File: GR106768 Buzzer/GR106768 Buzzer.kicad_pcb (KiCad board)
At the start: 4 copper layers, 76 x 58 mm, 175 parts, among them IC1 L-BC-SOT23-5, IC2 L-BC-SO08, IC3 L-BC-SO08, IC4 L-BC-SOT23-5, IC5 L-BC-SO08, IC6 L-BC-SO08, IC7 L-BC-SOT23-6, IC8 L-BC-DFN10, IC9 L-BC-SOT23-6, J1 BAR-10-1007, J2 MIRECMS, J3 MIRECMS, SW1 SI-10-NK236, T1 Q-BC-SOT23-BEC, T10 Q-BC-SOT23-GSD, T11 Q-BC-SOT23-GSD, T12 Q-BC-SOT23-GSD, T13 Q-BC-SOT23-GSD, T2 Q-BC-SOT23-BEC, T3 Q-BC-SOT23-BEC, T4 Q-BC-SOT23-BEC, T5 Q-BC-SOT23-GSD, T6 Q-BC-SOT23-GSD, T7 Q-BC-SOT23-GSD, T8 Q-BC-SOT23-GSD, T9 Q-BC-SOT23-GSD

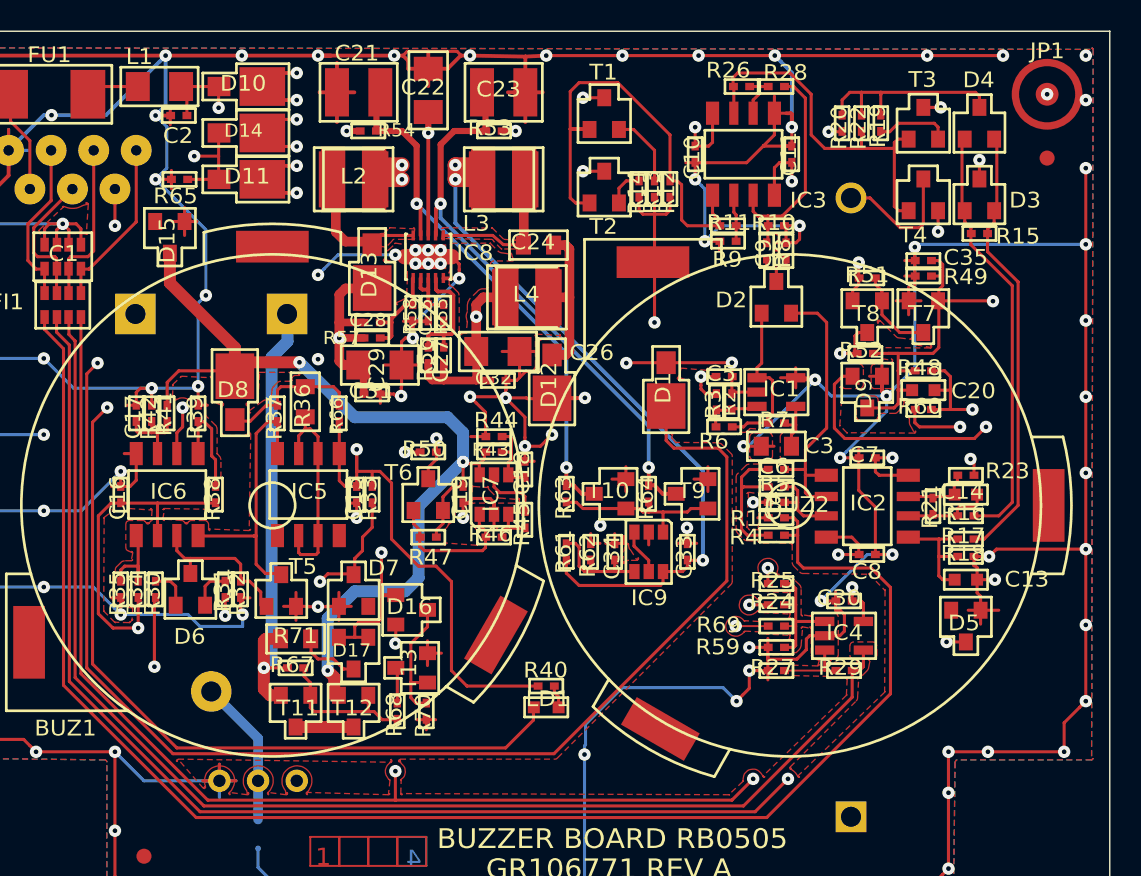
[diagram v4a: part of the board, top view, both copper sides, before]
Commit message: buzzer board custom via footprints
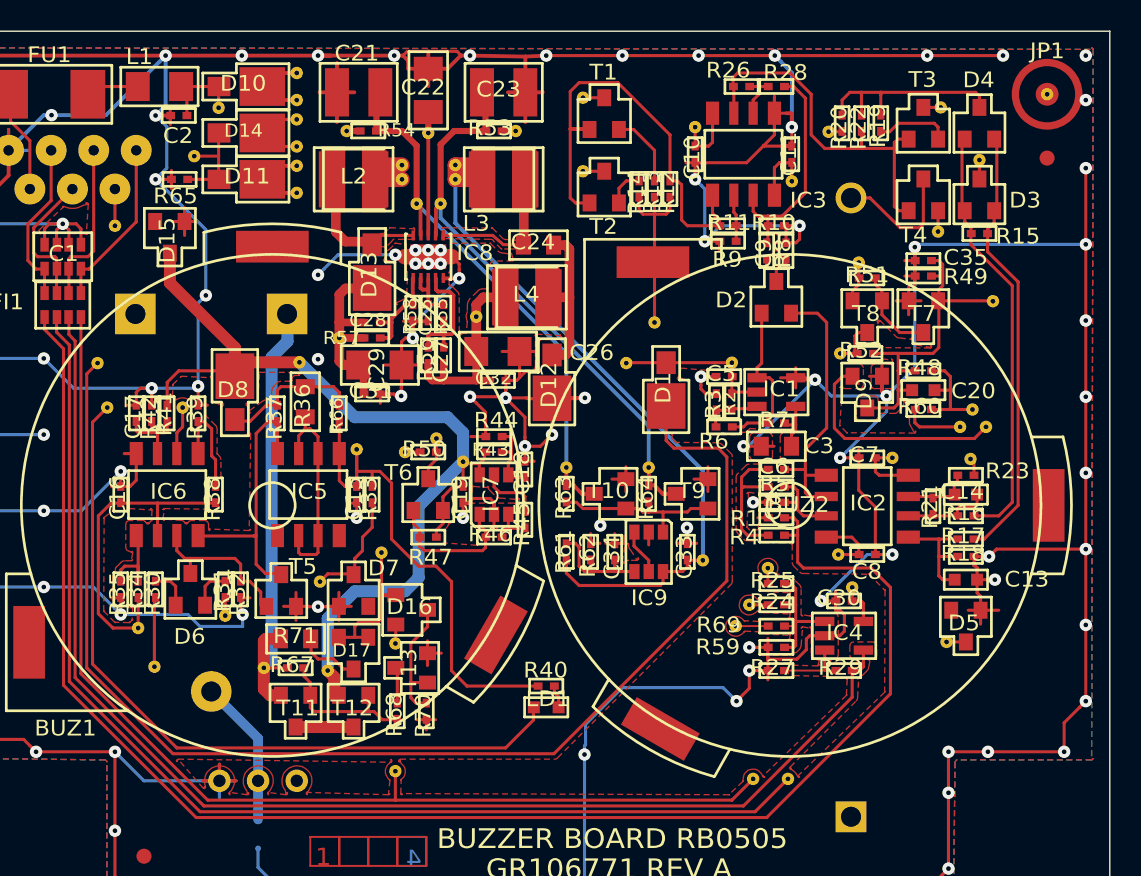
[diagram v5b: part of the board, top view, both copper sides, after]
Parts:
- added V1: +5V, AllModules:Via_12x32-1._.3.4, F.Cu at (143.2, 99.6)
- added V10: SUPPLY-BUZ-CPU, AllModules:Via_12x32-1._.3.4, F.Cu at (125.7, 78.2)
- added V11: SUPPLY-BUZ-CPU, AllModules:Via_12x32-1._.3.4, F.Cu at (124.6, 87.2)
- added V12: -12V, AllModules:Via_12x32-1._.3.4, F.Cu at (156.4, 74.6)
- added V13: -12V, AllModules:Via_12x32-1._.3.4, F.Cu at (170.1, 75.2)
- added V14: -12V, AllModules:Via_12x32-1._.3.4, F.Cu at (149.4, 84.1)
- added V15: -12V, AllModules:Via_12x32-1._.3.4, F.Cu at (173.2, 99.8)
- added V16: N$78, AllModules:Via_12x32-1._.3.4, F.Cu at (130.1, 90.1)
- added V17: N$78, AllModules:Via_12x32-1._.3.4, F.Cu at (125.2, 90.1)
- added V18: N$58, AllModules:Via_12x32-1._.3.4, F.Cu at (139.2, 101.5)
- added V19: N$58, AllModules:Via_12x32-1._.3.4, F.Cu at (127.2, 104.6)
- added V2: +5V, AllModules:Via_12x32-1._.3.4, F.Cu at (132.5, 70.4)
- added V20: N$31, AllModules:Via_12x32-1._.3.4, F.Cu at (182.5, 73.8)
- added V21: GT1, AllModules:Via_12x32-1._.3.4, F.Cu at (183.4, 83.1)
- added V22: GT1, AllModules:Via_12x32-1._.3.4, F.Cu at (186.9, 69.5)
- added V23: +12V, AllModules:Via_12x32-1._.3.4, F.Cu at (156.4, 69.8)
- added V24: +12V, AllModules:Via_12x32-1._.3.4, F.Cu at (179.9, 70.4)
- added V25: +12V, AllModules:Via_12x32-1._.3.4, F.Cu at (163.8, 71.7)
- added V26: +12V, AllModules:Via_12x32-1._.3.4, F.Cu at (140.4, 85.5)
- added V27: +12V, AllModules:Via_12x32-1._.3.4, F.Cu at (141.6, 92.8)
- added V28: +12V, AllModules:Via_12x32-1._.3.4, F.Cu at (176.8, 93.4)
- added V29: BATTV, AllModules:Via_12x32-1._._.4, F.Cu at (135.5, 107.2)
- added V3: +5V, AllModules:Via_12x32-1._.3.4, F.Cu at (181.2, 91.4)
- added V30: N$19, AllModules:Via_12x32-1._.3.4, F.Cu at (161.1, 84.5)
- added V31: N$18, AllModules:Via_12x32-1._.3.4, F.Cu at (172.6, 72.0)
- added V32: N$18, AllModules:Via_12x32-1._.3.4, F.Cu at (179.7, 78.5)
- added V33: N$10, AllModules:Via_12x32-1._._.4, F.Cu at (164.3, 100.1)
- added V34: N$10, AllModules:Via_12x32-1._.3.4, F.Cu at (148.0, 75.1)
- added V35: N$10, AllModules:Via_12x32-1._.3.4, F.Cu at (144.5, 75.1)
- added V36: N$10, AllModules:Via_12x32-1._.3.4, F.Cu at (144.5, 74.2)
- added V37: N$10, AllModules:Via_12x32-1._.3.4, F.Cu at (140.9, 71.9)
- added V38: N$10, AllModules:Via_12x32-1._.3.4, F.Cu at (146.3, 72.1)
- added V39: N$10, AllModules:Via_12x32-1._.3.4, F.Cu at (152.0, 71.9)
- added V4: +5V, AllModules:Via_12x32-1._.3.4, F.Cu at (144.7, 93.0)
- added V40: N$10, AllModules:Via_12x32-1._.3.4, F.Cu at (148.0, 74.2)
- added V41: N$10, AllModules:Via_12x32-1._.3.4, F.Cu at (137.6, 68.1)
- added V42: N$10, AllModules:Via_12x32-1._.3.4, F.Cu at (137.6, 69.9)
- added V43: N$10, AllModules:Via_12x32-1._.3.4, F.Cu at (137.6, 71.2)
- added V44: N$10, AllModules:Via_12x32-1._.3.4, F.Cu at (137.6, 73.0)
- added V45: N$10, AllModules:Via_12x32-1._.3.4, F.Cu at (137.6, 74.2)
- added V46: N$10, AllModules:Via_12x32-1._.3.4, F.Cu at (137.6, 76.0)
- added V47: STOP-INV, AllModules:Via_12x32-1._.3.4, F.Cu at (182.0, 90.2)
- added V48: STOP-INV, AllModules:Via_12x32-1._.3.4, F.Cu at (169.9, 114.5)
- added V49: VCHARG, AllModules:Via_12x32-1._._.4, F.Cu at (137.8, 87.1)
- added V5: +5V, AllModules:Via_12x32-1._.3.4, F.Cu at (174.1, 101.9)
- added V50: VCHARG, AllModules:Via_12x32-1._.3.4, F.Cu at (166.5, 104.5)
- added V51: VCHARG, AllModules:Via_12x32-1._.3.4, F.Cu at (139.7, 107.4)
- added V52: VCHARG, AllModules:Via_12x32-1._._.4, F.Cu at (148.6, 93.7)
- added V53: VBAT, AllModules:Via_12x32-1._.3.4, F.Cu at (174.5, 80.6)
- added V54: VBAT, AllModules:Via_12x32-1._.3.4, F.Cu at (146.8, 92.1)
- added V55: VBAT, AllModules:Via_12x32-1._.3.4, F.Cu at (168.6, 100.6)
- added V56: SUPPLY-BUZ, AllModules:Via_12x32-1._.3.4, F.Cu at (130.9, 73.6)
- added V57: SUPPLY-BUZ, AllModules:Via_12x32-1._.3.4, F.Cu at (173.3, 86.5)
- added V58: SUPPLY-BUZ, AllModules:Via_12x32-1._.3.4, F.Cu at (166.2, 87.2)
- added V59: SUPPLY-BUZ, AllModules:Via_12x32-1._.3.4, F.Cu at (159.3, 87.2)
- added V6: BUZ-ACT, AllModules:Via_12x32-1._.3.4, F.Cu at (128.3, 107.1)
- added V60: SUPPLY-BUZ, AllModules:Via_12x32-1._.3.4, F.Cu at (132.9, 103.8)
- added V61: SHDN2, AllModules:Via_12x32-1._._.4, F.Cu at (160.7, 94.0)
- added V62: SHDN2, AllModules:Via_12x32-1._._.4, F.Cu at (147.1, 76.7)
- added V63: SHDN1, AllModules:Via_12x32-1._._.4, F.Cu at (155.3, 94.0)
- added V64: SHDN1, AllModules:Via_12x32-1._._.4, F.Cu at (145.5, 76.7)
- added V65: INHIB-STOP-INV, AllModules:Via_12x32-1._.3.4, F.Cu at (144.1, 114.0)
- added V66: INHIB-STOP-INV, AllModules:Via_12x32-1._.3.4, F.Cu at (144.1, 105.6)
- added V67: INHIB-STOP-INV, AllModules:Via_12x32-1._.3.4, F.Cu at (182.9, 91.4)
- added V68: INHIB-STOP-INV, AllModules:Via_12x32-1._.3.4, F.Cu at (167.6, 114.5)
- added V7: BUZ-ACT, AllModules:Via_12x32-1._.3.4, F.Cu at (181.9, 93.5)
- added V8: BUZ-ACT, AllModules:Via_12x32-1._.3.4, F.Cu at (167.4, 103.1)
- added V9: BUZ-ACT, AllModules:Via_12x32-1._.3.4, F.Cu at (180.3, 105.5)
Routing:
- net VCHARG: vias 4 -> 0
- net VBAT: vias 3 -> 0
- net SUPPLY-BUZ-CPU: vias 2 -> 0
- net SUPPLY-BUZ: vias 5 -> 0
- net STOP-INV: vias 2 -> 0
- net SHDN2: vias 2 -> 0
- net SHDN1: vias 2 -> 0
- net N$78: vias 2 -> 0
- net N$58: vias 2 -> 0
- net N$31: vias 1 -> 0
- net N$19: vias 1 -> 0
- net N$18: vias 2 -> 0
- net N$10: vias 14 -> 0
- net INHIB-STOP-INV: vias 4 -> 0
- net GT1: vias 2 -> 0
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
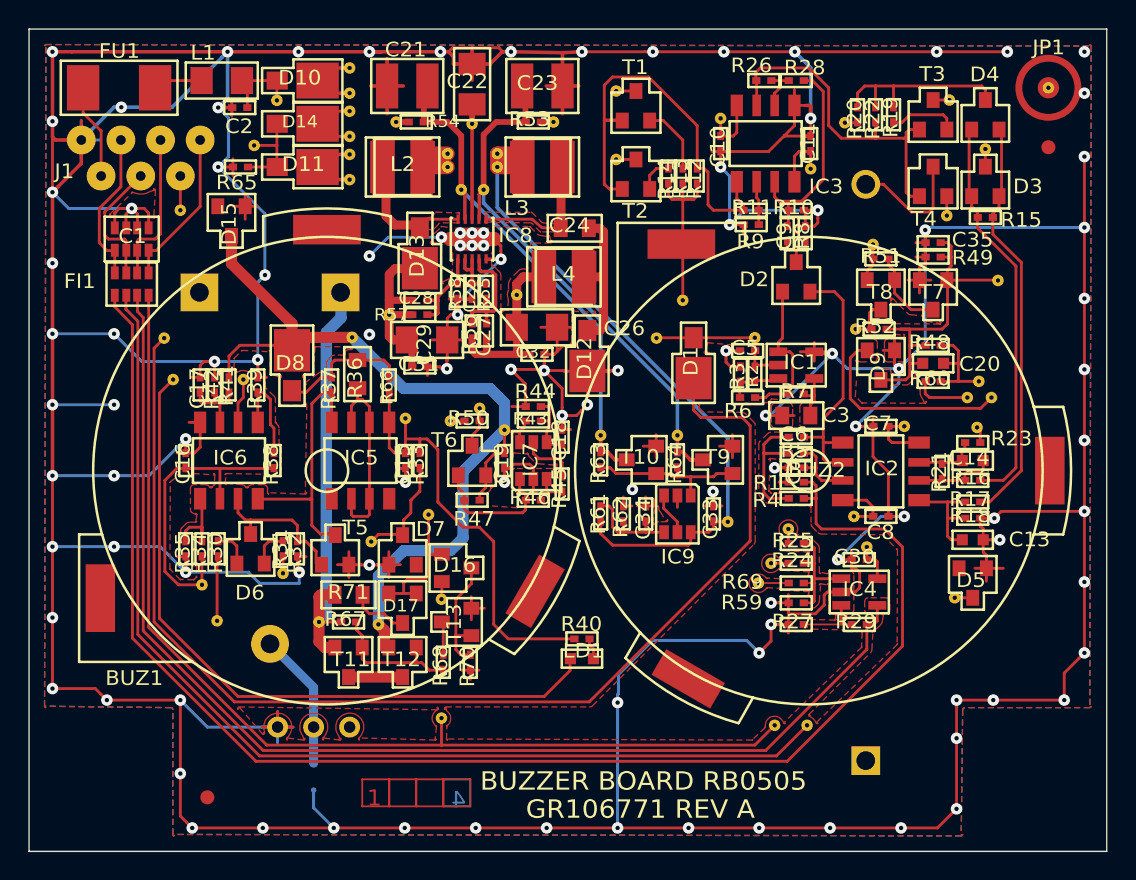
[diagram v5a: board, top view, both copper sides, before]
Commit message: fixed some PCB zones
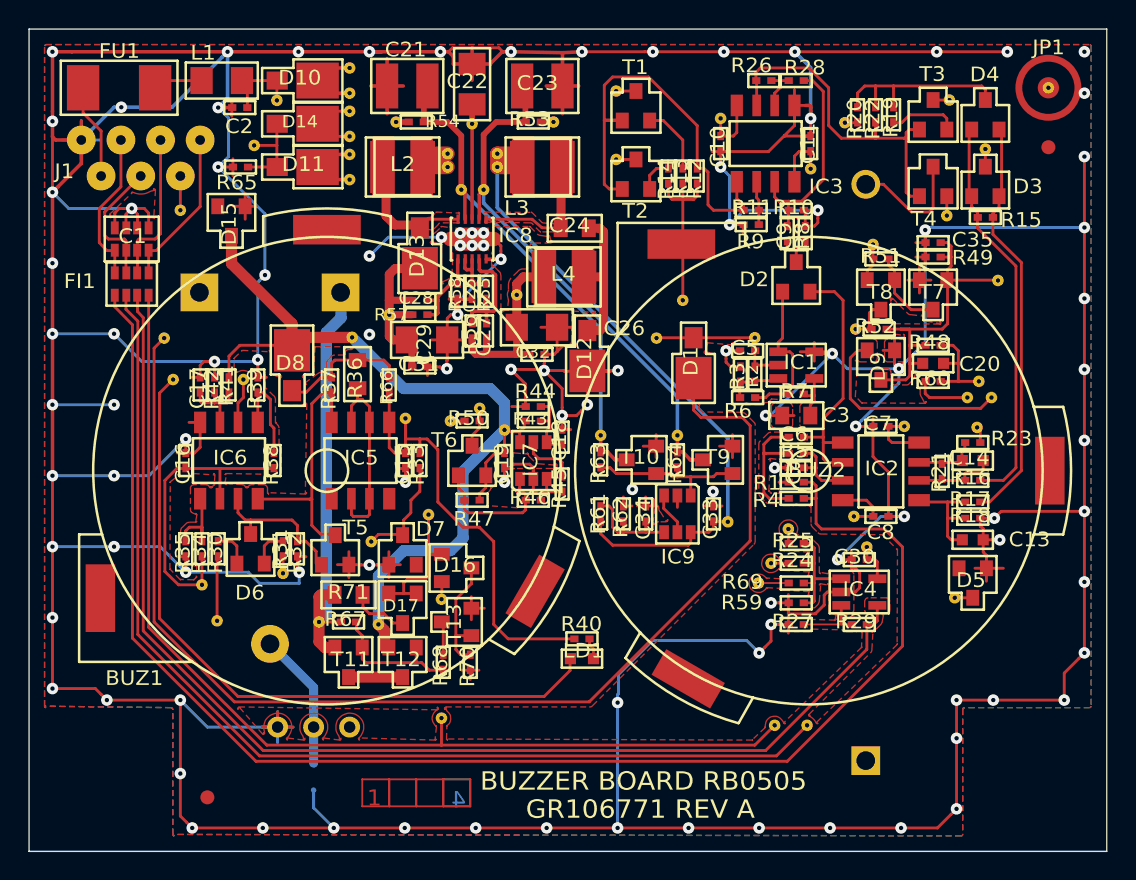
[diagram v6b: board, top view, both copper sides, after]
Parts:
- removed CAM1: A3_EQFC_COVIDIEN, A3_EQFC_COVIDIEN_1
- removed CAM12: FABRICATION, FABRICATION_1
- removed CAM13: PERCAGE_TABLEAU, PERCAGE_TABLEAU_1
- removed CAM14: A3_PER_COVIDIEN, A3_PER_COVIDIEN_1
- removed CAM2: PER-COVIDIEN_TEXTE, PER-COVIDIEN_TEXTE_1
- removed CAM3: A3_EQFS_COVIDIEN, A3_EQFS_COVIDIEN_1
- removed CAM5: FILM13_HORIZONTAL, FILM13_HORIZONTAL_1
- removed CAM6, CAM7, CAM8, CAM9: COIN_EXTERNE, COIN_EXTERNE_1
